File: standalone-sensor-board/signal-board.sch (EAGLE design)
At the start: 19 parts, among them U1 CD4051BE

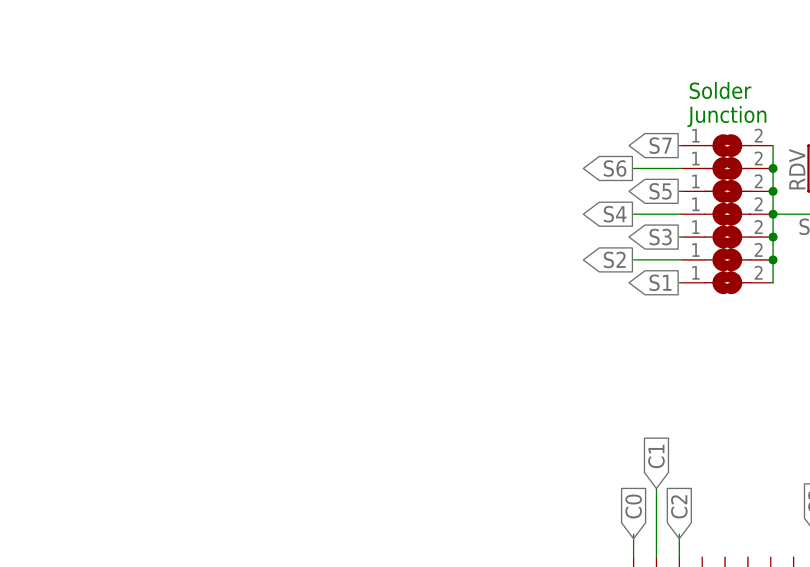
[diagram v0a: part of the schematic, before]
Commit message: add divider resistors
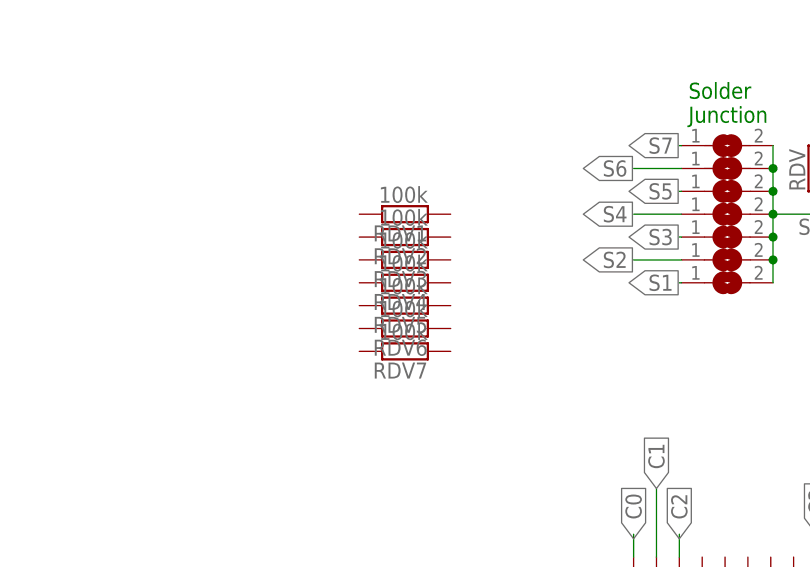
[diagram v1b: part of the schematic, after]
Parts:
- added RDV1, RDV2, RDV3, RDV4, RDV5, RDV6, RDV7: 100k, rcl:R-EU_0207/10
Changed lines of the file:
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@@
 <part name="J3" library="686114148922" deviceset="686114148922" device=""/>
 <part name="J4" library="686114148922" deviceset="686114148922" device=""/>
+<part name="RDV1" library="rcl" library_urn="urn:adsk.eagle:library:334" deviceset="R-EU_" device="0207/10" package3d_urn="urn:adsk.eagle:package:23491/2" value="100k"/>
+<part name="RDV2" library="rcl" library_urn="urn:adsk.eagle:library:334" deviceset="R-EU_" device="0207/10" package3d_urn="urn:adsk.eagle:package:23491/2" value="100k"/>
+<part name="RDV3" library="rcl" library_urn="urn:adsk.eagle:library:334" deviceset="R-EU_" device="0207/10" package3d_urn="urn:adsk.eagle:package:23491/2" value="100k"/>
+<part name="RDV4" library="rcl" library_urn="urn:adsk.eagle:library:334" deviceset="R-EU_" device="0207/10" package3d_urn="urn:adsk.eagle:package:23491/2" value="100k"/>
+<part name="RDV5" library="rcl" library_urn="urn:adsk.eagle:library:334" deviceset="R-EU_" device="0207/10" package3d_urn="urn:adsk.eagle:package:23491/2" value="100k"/>
+<part name="RDV6" library="rcl" library_urn="urn:adsk.eagle:library:334" deviceset="R-EU_" device="0207/10" package3d_urn="urn:adsk.eagle:package:23491/2" value="100k"/>
+<part name="RDV7" library="rcl" library_urn="urn:adsk.eagle:library:334" deviceset="R-EU_" device="0207/10" package3d_urn="urn:adsk.eagle:package:23491/2" value="100k"/>
 </parts>
 <sheets>
@@
 <attribute name="VALUE" x="-34.29" y="83.82" size="1.778" layer="96" rot="MR180" align="center-left"/>
 </instance>
+<instance part="RDV1" gate="G$1" x="5.08" y="38.1" smashed="yes" rot="R180">
+<attribute name="NAME" x="7.62" y="36.8554" size="1.778" layer="95" rot="R180"/>
+<attribute name="VALUE" x="7.62" y="41.148" size="1.778" layer="96" rot="R180"/>
+</instance>
+<instance part="RDV2" gate="G$1" x="5.08" y="35.56" smashed="yes" rot="R180">
+<attribute name="NAME" x="7.62" y="34.3154" size="1.778" layer="95" rot="R180"/>
+<attribute name="VALUE" x="7.62" y="38.608" size="1.778" layer="96" rot="R180"/>
+</instance>
+<instance part="RDV3" gate="G$1" x="5.08" y="33.02" smashed="yes" rot="R180">
+<attribute name="NAME" x="7.62" y="31.7754" size="1.778" layer="95" rot="R180"/>
+<attribute name="VALUE" x="7.62" y="36.068" size="1.778" layer="96" rot="R180"/>
+</instance>
+<instance part="RDV4" gate="G$1" x="5.08" y="30.48" smashed="yes" rot="R180">
+<attribute name="NAME" x="7.62" y="29.2354" size="1.778" layer="95" rot="R180"/>
+<attribute name="VALUE" x="7.62" y="33.528" size="1.778" layer="96" rot="R180"/>
+</instance>
+<instance part="RDV5" gate="G$1" x="5.08" y="27.94" smashed="yes" rot="R180">
+<attribute name="NAME" x="7.62" y="26.6954" size="1.778" layer="95" rot="R180"/>
+<attribute name="VALUE" x="7.62" y="30.988" size="1.778" layer="96" rot="R180"/>
+</instance>
+<instance part="RDV6" gate="G$1" x="5.08" y="25.4" smashed="yes" rot="R180">
+<attribute name="NAME" x="7.62" y="24.1554" size="1.778" layer="95" rot="R180"/>
+<attribute name="VALUE" x="7.62" y="28.448" size="1.778" layer="96" rot="R180"/>
+</instance>
+<instance part="RDV7" gate="G$1" x="5.08" y="22.86" smashed="yes" rot="R180">
+<attribute name="NAME" x="7.62" y="21.6154" size="1.778" layer="95" rot="R180"/>
+<attribute name="VALUE" x="7.62" y="25.908" size="1.778" layer="96" rot="R180"/>
+</instance>
 </instances>

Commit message: set rdvs
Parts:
- removed D1, D2, D3, D4, D5, D6, D7: 1655, 1655:1655
- removed RDV: 100k, rcl:R-EU_0207/10
- added LED1, LED2, LED3, LED4, LED5, LED6, LED7: WS2812B3535, adafruit:WS2812B3535
- J1: value (none) -> sensors
- J3: value (none) -> to_next_board
- J4: value (none) -> to_controller
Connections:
- removed net N$15: D6.DOUT, D7.DIN
- removed net N$16: D1.DOUT, D2.DIN
- removed net N$17: D2.DOUT, D3.DIN
- removed net N$18: D3.DOUT, D4.DIN
- removed net N$19: D4.DOUT, D5.DIN
- removed net N$20: D5.DOUT, D6.DIN
- new net N$1: LED1.DO, LED2.DI
- new net N$2: LED2.DO, LED3.DI
- new net N$3: LED3.DO, LED4.DI
- new net N$4: LED4.DO, LED5.DI
- new net N$5: LED5.DO, LED6.DI
- new net N$6: LED6.DO, LED7.DI
- net 3V: now also LED1.VDD, LED2.VDD, LED3.VDD, LED4.VDD, LED5.VDD, LED6.VDD, LED7.VDD; no longer D1.VDD, D2.VDD, D3.VDD, D4.VDD, D5.VDD, D6.VDD, D7.VDD
- net C0: now also RDV1.2
- net C1: now also RDV2.2
- net C2: now also RDV3.2
- net C3: now also RDV4.2
- net C4: now also RDV5.2
- net C5: now also RDV6.2
- net C6: now also RDV7.2
- net DIN: now also LED1.DI; no longer D1.DIN
- net DOUT: now also LED7.DO; no longer D7.DOUT
- net GND: now also LED1.GND, LED2.GND, LED3.GND, LED4.GND, LED5.GND, LED6.GND, LED7.GND; no longer D1.VSS, D2.VSS, D3.VSS, D4.VSS, D5.VSS, D6.VSS, D7.VSS
- net SIG: no longer RDV.1
- net VCC: now also RDV1.1, RDV2.1, RDV3.1, RDV4.1, RDV5.1, RDV6.1, RDV7.1; no longer RDV.2
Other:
- moved on the sheet: J1, RDV1, RDV2, RDV3, RDV4, RDV5, RDV6, RDV7

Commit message: signal board routing
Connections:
- net 3V: now also J3.2; no longer J3.13
- net A: now also J3.4; no longer J3.11
- net B: now also J3.5; no longer J3.10
- net C: now also J3.6; no longer J3.9
- net DOUT: now also J3.7; no longer J3.8
- net GND: now also J3.1; no longer J3.14
- net S1: now also J3.8; no longer J3.7
- net S2: now also J3.9; no longer J3.6
- net S3: now also J3.10; no longer J3.5
- net S4: now also J3.11; no longer J3.4
- net S5: now also J3.12; no longer J3.3
- net S6: now also J3.13; no longer J3.2
- net S7: now also J3.14; no longer J3.1
- net VCC: now also J3.3; no longer J3.12
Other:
- moved on the sheet: J3
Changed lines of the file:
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@@
 <attribute name="VALUE" x="85.8774" y="21.8186" size="2.0828" layer="96" ratio="6" rot="SMR0"/>
 </instance>
-<instance part="SUPPLY10" gate="G$1" x="71.12" y="83.82" smashed="yes">
-<attribute name="VALUE" x="69.723" y="86.741" size="1.778" layer="96"/>
+<instance part="SUPPLY10" gate="G$1" x="71.12" y="127" smashed="yes">
+<attribute name="VALUE" x="69.723" y="129.921" size="1.778" layer="96"/>
 </instance>
 <instance part="GND2" gate="1" x="68.58" y="-71.12" smashed="yes" rot="MR0">
@@
 <attribute name="VALUE" x="25.4" y="-44.45" size="1.778" layer="96" rot="R90" align="center-left"/>
 </instance>
-<instance part="J3" gate="G$1" x="162.56" y="88.9" smashed="yes" rot="R180">
-<attribute name="NAME" x="163.83" y="86.36" size="1.778" layer="95" rot="R180" align="center-left"/>
-<attribute name="VALUE" x="140.97" y="83.82" size="1.778" layer="96" rot="R180" align="center-left"/>
+<instance part="J3" gate="G$1" x="190.5" y="121.92" smashed="yes" rot="MR0">
+<attribute name="NAME" x="191.77" y="124.46" size="1.778" layer="95" rot="MR0" align="center-left"/>
+<attribute name="VALUE" x="168.91" y="127" size="1.778" layer="96" rot="MR0" align="center-left"/>
 </instance>
 <instance part="J4" gate="G$1" x="-55.88" y="88.9" smashed="yes" rot="MR180">
@@
 <junction x="-55.88" y="91.44"/>
 <wire x1="-27.94" y1="127" x2="-27.94" y2="121.92" width="0.1524" layer="91"/>
+<junction x="-27.94" y="121.92"/>
+<pinref part="J3" gate="G$1" pin="MP2"/>
 <pinref part="J3" gate="G$1" pin="MP1"/>
-<pinref part="J3" gate="G$1" pin="MP2"/>
-<wire x1="162.56" y1="88.9" x2="162.56" y2="91.44" width="0.1524" layer="91"/>
-<wire x1="162.56" y1="91.44" x2="162.56" y2="127" width="0.1524" layer="91"/>
-<junction x="162.56" y="91.44"/>
-<pinref part="J3" gate="G$1" pin="14"/>
-<wire x1="162.56" y1="127" x2="137.16" y2="127" width="0.1524" layer="91"/>
-<wire x1="137.16" y1="127" x2="137.16" y2="121.92" width="0.1524" layer="91"/>
-<wire x1="137.16" y1="121.92" x2="-27.94" y2="121.92" width="0.1524" layer="91"/>
-<junction x="137.16" y="121.92"/>
-<junction x="-27.94" y="121.92"/>
+<wire x1="190.5" y1="121.92" x2="190.5" y2="119.38" width="0.1524" layer="91"/>
+<wire x1="190.5" y1="121.92" x2="190.5" y2="127" width="0.1524" layer="91"/>
+<junction x="190.5" y="121.92"/>
+<wire x1="190.5" y1="127" x2="165.1" y2="127" width="0.1524" layer="91"/>
+<pinref part="J3" gate="G$1" pin="1"/>
+<wire x1="165.1" y1="127" x2="165.1" y2="121.92" width="0.1524" layer="91"/>
+<wire x1="165.1" y1="121.92" x2="-27.94" y2="121.92" width="0.1524" layer="91"/>
+<junction x="165.1" y="121.92"/>
 </segment>
 </net>
@@
 <pinref part="J4" gate="G$1" pin="11"/>
 <label x="-27.94" y="114.3" size="1.778" layer="95" xref="yes"/>
-<pinref part="J3" gate="G$1" pin="11"/>
-<wire x1="-30.48" y1="114.3" x2="137.16" y2="114.3" width="0.1524" layer="91"/>
+<pinref part="J3" gate="G$1" pin="4"/>
+<wire x1="-30.48" y1="114.3" x2="165.1" y2="114.3" width="0.1524" layer="91"/>
 </segment>
 </net>
@@
 <pinref part="J4" gate="G$1" pin="10"/>
 <label x="-27.94" y="111.76" size="1.778" layer="95" xref="yes"/>
-<pinref part="J3" gate="G$1" pin="10"/>
-<wire x1="137.16" y1="111.76" x2="-30.48" y2="111.76" width="0.1524" layer="91"/>
+<pinref part="J3" gate="G$1" pin="5"/>
+<wire x1="-30.48" y1="111.76" x2="165.1" y2="111.76" width="0.1524" layer="91"/>
 </segment>
 </net>
@@
 <pinref part="J4" gate="G$1" pin="9"/>
 <label x="-27.94" y="109.22" size="1.778" layer="95" xref="yes"/>
-<pinref part="J3" gate="G$1" pin="9"/>
-<wire x1="-30.48" y1="109.22" x2="137.16" y2="109.22" width="0.1524" layer="91"/>
+<pinref part="J3" gate="G$1" pin="6"/>
+<wire x1="-30.48" y1="109.22" x2="165.1" y2="109.22" width="0.1524" layer="91"/>
 </segment>
 </net>
@@
 <net name="DOUT" class="0">
 <segment>
-<pinref part="J3" gate="G$1" pin="8"/>
-<wire x1="134.62" y1="106.68" x2="137.16" y2="106.68" width="0.1524" layer="91"/>
 <pinref part="LED7" gate="G$1" pin="DO"/>
 <wire x1="149.86" y1="142.24" x2="149.86" y2="132.08" width="0.1524" layer="91"/>
-<wire x1="149.86" y1="132.08" x2="119.38" y2="132.08" width="0.1524" layer="91"/>
-<wire x1="119.38" y1="132.08" x2="119.38" y2="106.68" width="0.1524" layer="91"/>
-<wire x1="119.38" y1="106.68" x2="137.16" y2="106.68" width="0.1524" layer="91"/>
-<junction x="137.16" y="106.68"/>
+<wire x1="149.86" y1="132.08" x2="121.92" y2="132.08" width="0.1524" layer="91"/>
+<wire x1="121.92" y1="132.08" x2="121.92" y2="106.68" width="0.1524" layer="91"/>
+<pinref part="J3" gate="G$1" pin="7"/>
+<wire x1="121.92" y1="106.68" x2="165.1" y2="106.68" width="0.1524" layer="91"/>
 </segment>
 </net>
@@
 <pinref part="J4" gate="G$1" pin="6"/>
 <label x="-27.94" y="101.6" size="1.778" layer="95" xref="yes"/>
-<pinref part="J3" gate="G$1" pin="6"/>
-<wire x1="-30.48" y1="101.6" x2="137.16" y2="101.6" width="0.1524" layer="91"/>
+<pinref part="J3" gate="G$1" pin="9"/>
+<wire x1="-30.48" y1="101.6" x2="165.1" y2="101.6" width="0.1524" layer="91"/>
 </segment>
 </net>
@@
 <pinref part="J4" gate="G$1" pin="4"/>
 <label x="-27.94" y="96.52" size="1.778" layer="95" xref="yes"/>
-<pinref part="J3" gate="G$1" pin="4"/>
-<wire x1="137.16" y1="96.52" x2="-30.48" y2="96.52" width="0.1524" layer="91"/>
+<pinref part="J3" gate="G$1" pin="11"/>
+<wire x1="-30.48" y1="96.52" x2="165.1" y2="96.52" width="0.1524" layer="91"/>
 </segment>
 </net>
@@
 <wire x1="91.44" y1="48.26" x2="96.52" y2="48.26" width="0.1524" layer="91"/>
 <pinref part="U1" gate="A" pin="VDD"/>
-<wire x1="91.44" y1="55.88" x2="91.44" y2="48.26" width="0.1524" layer="91"/>
-<junction x="91.44" y="48.26"/>
 <pinref part="SUPPLY8" gate="G$1" pin="VCC"/>
 </segment>
@@
 <pinref part="J4" gate="G$1" pin="12"/>
 <label x="-27.94" y="116.84" size="1.778" layer="95" xref="yes"/>
-<pinref part="J3" gate="G$1" pin="12"/>
-<wire x1="137.16" y1="116.84" x2="-30.48" y2="116.84" width="0.1524" layer="91"/>
+<pinref part="J3" gate="G$1" pin="3"/>
+<wire x1="-30.48" y1="116.84" x2="165.1" y2="116.84" width="0.1524" layer="91"/>
 </segment>
 </net>
@@
 <segment>
 <pinref part="SUPPLY10" gate="G$1" pin="3V"/>
-<wire x1="10.16" y1="81.28" x2="71.12" y2="81.28" width="0.1524" layer="91"/>
-<junction x="71.12" y="81.28"/>
-<wire x1="132.08" y1="81.28" x2="71.12" y2="81.28" width="0.1524" layer="91"/>
+<wire x1="10.16" y1="124.46" x2="71.12" y2="124.46" width="0.1524" layer="91"/>
+<junction x="71.12" y="124.46"/>
+<wire x1="132.08" y1="124.46" x2="71.12" y2="124.46" width="0.1524" layer="91"/>
 <pinref part="J4" gate="G$1" pin="13"/>
 <label x="-27.94" y="119.38" size="1.778" layer="95" xref="yes"/>
-<pinref part="J3" gate="G$1" pin="13"/>
 <wire x1="-30.48" y1="119.38" x2="-25.4" y2="119.38" width="0.1524" layer="91"/>
 <wire x1="-25.4" y1="119.38" x2="10.16" y2="119.38" width="0.1524" layer="91"/>
-<wire x1="132.08" y1="119.38" x2="137.16" y2="119.38" width="0.1524" layer="91"/>
-<wire x1="10.16" y1="81.28" x2="10.16" y2="119.38" width="0.1524" layer="91"/>
-<wire x1="132.08" y1="81.28" x2="132.08" y2="119.38" width="0.1524" layer="91"/>
+<wire x1="10.16" y1="124.46" x2="10.16" y2="119.38" width="0.1524" layer="91"/>
+<wire x1="132.08" y1="124.46" x2="132.08" y2="129.54" width="0.1524" layer="91"/>
 <wire x1="-25.4" y1="119.38" x2="-25.4" y2="132.08" width="0.1524" layer="91"/>
 <junction x="-25.4" y="119.38"/>
@@
 <wire x1="-35.56" y1="160.02" x2="-10.16" y2="160.02" width="0.1524" layer="91"/>
 <junction x="-10.16" y="160.02"/>
-<wire x1="132.08" y1="119.38" x2="132.08" y2="129.54" width="0.1524" layer="91"/>
-<junction x="132.08" y="119.38"/>
 <wire x1="132.08" y1="129.54" x2="157.48" y2="129.54" width="0.1524" layer="91"/>
 <wire x1="157.48" y1="129.54" x2="157.48" y2="160.02" width="0.1524" layer="91"/>
 <wire x1="157.48" y1="160.02" x2="142.24" y2="160.02" width="0.1524" layer="91"/>
 <junction x="142.24" y="160.02"/>
+<pinref part="J3" gate="G$1" pin="2"/>
+<wire x1="132.08" y1="119.38" x2="165.1" y2="119.38" width="0.1524" layer="91"/>
+<wire x1="132.08" y1="124.46" x2="132.08" y2="119.38" width="0.1524" layer="91"/>
+<junction x="132.08" y="124.46"/>
 </segment>
 </net>
@@
 <pinref part="J4" gate="G$1" pin="3"/>
 <label x="-27.94" y="93.98" size="1.778" layer="95" xref="yes"/>
-<pinref part="J3" gate="G$1" pin="3"/>
-<wire x1="-30.48" y1="93.98" x2="137.16" y2="93.98" width="0.1524" layer="91"/>
+<pinref part="J3" gate="G$1" pin="12"/>
+<wire x1="-30.48" y1="93.98" x2="165.1" y2="93.98" width="0.1524" layer="91"/>
 </segment>
 </net>
@@
 <pinref part="J4" gate="G$1" pin="7"/>
 <label x="-27.94" y="104.14" size="1.778" layer="95" xref="yes"/>
-<pinref part="J3" gate="G$1" pin="7"/>
-<wire x1="137.16" y1="104.14" x2="-30.48" y2="104.14" width="0.1524" layer="91"/>
+<pinref part="J3" gate="G$1" pin="8"/>
+<wire x1="-30.48" y1="104.14" x2="165.1" y2="104.14" width="0.1524" layer="91"/>
 </segment>
 </net>
@@
 <pinref part="J4" gate="G$1" pin="5"/>
 <label x="-27.94" y="99.06" size="1.778" layer="95" xref="yes"/>
-<pinref part="J3" gate="G$1" pin="5"/>
-<wire x1="-30.48" y1="99.06" x2="137.16" y2="99.06" width="0.1524" layer="91"/>
+<pinref part="J3" gate="G$1" pin="10"/>
+<wire x1="-30.48" y1="99.06" x2="165.1" y2="99.06" width="0.1524" layer="91"/>
 </segment>
 </net>
@@
 <pinref part="J4" gate="G$1" pin="1"/>
 <label x="-27.94" y="88.9" size="1.778" layer="95" xref="yes"/>
-<pinref part="J3" gate="G$1" pin="1"/>
-<wire x1="-30.48" y1="88.9" x2="137.16" y2="88.9" width="0.1524" layer="91"/>
+<pinref part="J3" gate="G$1" pin="14"/>
+<wire x1="-30.48" y1="88.9" x2="165.1" y2="88.9" width="0.1524" layer="91"/>
 </segment>
 </net>
@@
 <pinref part="J4" gate="G$1" pin="2"/>
 <label x="-27.94" y="91.44" size="1.778" layer="95" xref="yes"/>
-<pinref part="J3" gate="G$1" pin="2"/>
-<wire x1="137.16" y1="91.44" x2="-30.48" y2="91.44" width="0.1524" layer="91"/>
-</segment>
-</net>
+<pinref part="J3" gate="G$1" pin="13"/>
+<wire x1="-30.48" y1="91.44" x2="165.1" y2="91.44" width="0.1524" layer="91"/>
+</segment>
+</net>
